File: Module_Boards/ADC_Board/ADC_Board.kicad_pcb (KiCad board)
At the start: 6 copper layers, 13 x 17.7 mm, 46 parts, among them J1 212134-0003, J2 212134-0003, J3 212134-0003, J4 212134-0003, U1 LTC1864LIMS8#PBF, U2 TXB0104RUTR, U3 TPS22916CYFPR, U4 TPS7A9401DSCR, U5 TMUX1104DQAR

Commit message: Big push. Fixed the issues that were pending. See github
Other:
- board text added: "CS"
- board text added: "MI"
- board text added: "SCK"
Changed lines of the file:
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@@
+	)
+	(gr_line
+		(start 130.2 86.5456)
+		(end 129.946 86.5456)
+		(stroke
+			(width 0.1)
+			(type default)
+		)
+		(layer "F.SilkS")
+	)
+	(gr_line
+		(start 140.990235 86.668504)
+		(end 141.334606 87.407011)
+		(stroke
+			(width 0.1)
+			(type default)
+		)
+		(layer "F.SilkS")
+	)
+	(gr_rect
+		(start 129.7 86.0356)
+		(end 129.9 87.0556)
+		(stroke
+			(width 0.1)
+			(type solid)
+		)
+		(fill solid)
+		(layer "F.SilkS")
+	)
+	(gr_line
+		(start 141.184137 87.038926)
+		(end 141.434869 86.788195)
+		(stroke
+			(width 0.1)
+			(type default)
+		)
+		(layer "F.SilkS")
+	)
+	(gr_line
+		(start 140.780535 86.809306)
+		(end 141.124907 87.547813)
+		(stroke
+			(width 0.1)
+			(type default)
+		)
+		(layer "F.SilkS")
+	)
+	(gr_poly
+		(pts
+			(xy 141.60188 89.015667) (xy 141.036196 89.128804) (xy 141.149333 88.56312)
+		)
+		(stroke
+			(width 0.1)
+			(type solid)
+		)
+		(fill solid)
+		(layer "F.SilkS")
+	)
+	(gr_line
+		(start 130.2 87.0536)
+		(end 130.2 86.0376)
+		(stroke
+			(width 0.1)
+			(type default)
+		)
+		(layer "F.SilkS")
+	)
+	(gr_line
+		(start 141.319039 88.845961)
+		(end 141.658449 88.506551)
+		(stroke
+			(width 0.2)
+			(type default)
+		)
+		(layer "F.SilkS")
+	)
+	(gr_line
+		(start 130.454 86.9266)
+		(end 130.454 86.1646)
+		(stroke
+			(width 0.1)
+			(type default)
+		)
+		(layer "F.SilkS")
+	)
+	(gr_line
+		(start 130.708 86.6726)
+		(end 130.708 86.4186)
+		(stroke
+			(width 0.1)
+			(type default)
+		)
+		(layer "F.SilkS")
+	)
+	(gr_rect
+		(start 141.1 84.7656)
+		(end 141.3 85.7856)
+		(stroke
+			(width 0.1)
+			(type solid)
+		)
+		(fill solid)
+		(layer "F.SilkS")
 	)
 	(gr_line
@@
 		)
 		(layer "Edge.Cuts")
+	)
+	(gr_text "CS"
+		(at 130.325269 85.863695 90)
+		(layer "F.SilkS")
+		(effects
+			(font
+				(size 0.5 0.5)
+				(thickness 0.1)
+				(bold yes)
+			)
+			(justify left bottom)
+		)
+	)
+	(gr_text "MI"
+		(at 130.325269 84.510362 90)
+		(layer "F.SilkS")
+		(effects
+			(font
+				(size 0.5 0.5)
+				(thickness 0.1)
+				(bold yes)
+			)
+			(justify left bottom)
+		)
+	)
+	(gr_text "SCK"
+		(at 130.325269 83.573695 90)
+		(layer "F.SilkS")
+		(effects
+			(font
+				(size 0.5 0.5)
+				(thickness 0.1)
+				(bold yes)
+			)
+			(justify left bottom)
+		)
 	)
 	(segment
@@
 		)
 	)
+	(group ""
+		(members "25f6bcfe-40dd-4638-9ee8-8388c1f33a2e" "b8615d0e-870a-46f8-8a8a-49a5995449ec"
+			"c08f6b8e-181b-46dc-a771-4c8004ccd757" "c74e4047-e888-4410-b1a2-d58da0c20ed8"
+		)
+	)

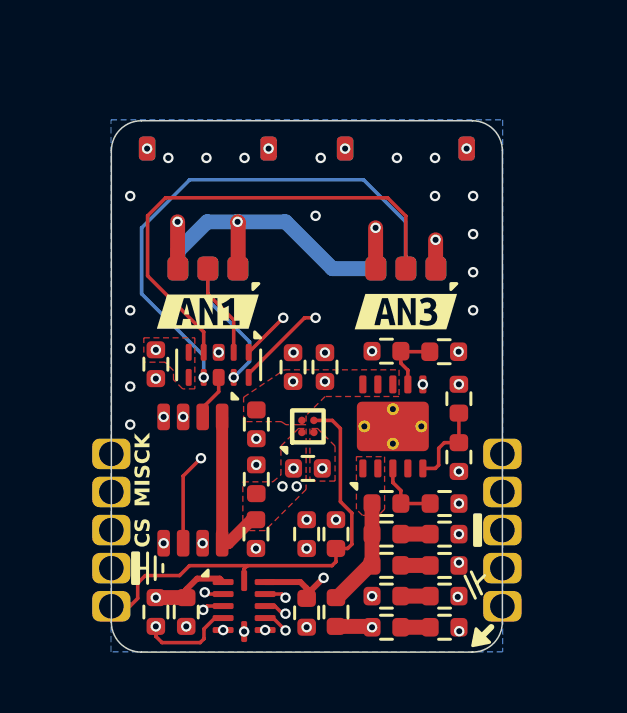
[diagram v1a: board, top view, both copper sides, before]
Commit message: Fixed bugs. Added comments. Push before changing the ADC
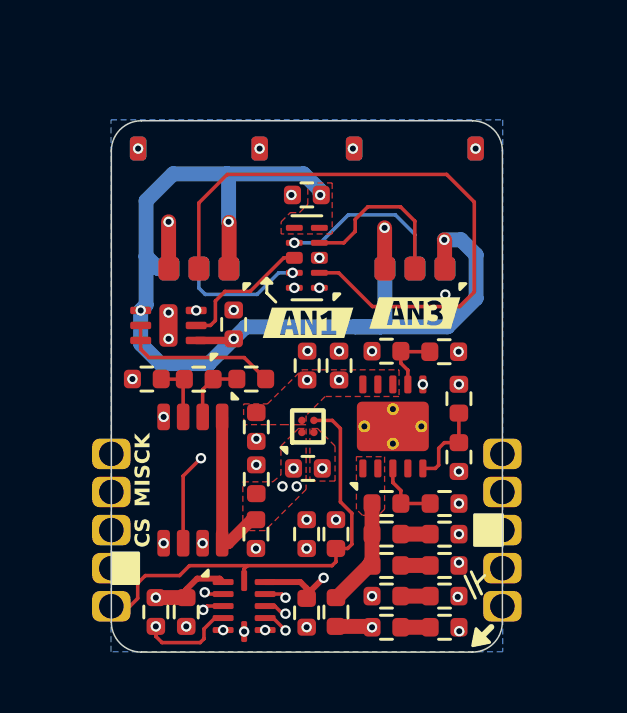
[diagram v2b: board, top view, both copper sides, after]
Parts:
- removed kibuzzard-67164525: G***, kibuzzard-67164525
- removed kibuzzard-6716453A: G***, kibuzzard-6716453A
- added C14: 2n20 25V, X-MODs_PcbLib:C0402, F.Cu at (131.9, 80.2)
- added C15: 100n 10V, X-MODs_PcbLib:C0402, F.Cu at (133.1, 78.4)
- added R1: 39R0, X-MODs_PcbLib:R0402, F.Cu at (130.2, 80.2)
- added R3: 39R0, X-MODs_PcbLib:R0402, F.Cu at (133.7, 80.2)
- added U6: LTC6255CS6#TRMPBF, X-MODs_PcbLib:DFN-6, F.Cu at (130.9, 78.5)
- added kibuzzard-674D683C: G***, kibuzzard-674D683C, F.Cu at (135.5, 78.4)
- added kibuzzard-674D6840: G***, kibuzzard-674D6840, F.Cu at (139.1, 78.0)
- C1: value 10u0 16V -> 2u20 16V
- C10, C6, C8: value 10u0 16V -> 22u0 6V3
- C7, C9: value 10u0 16V -> 10n0 16V
- FB1: value FerriteBead -> 300R
- R10, R12: value TBD -> 1R00
- R11, R9: value TBD -> 0R30
- R13, R15: value TBD -> 100K
- R7: value TBD -> 169K
- R8: value TBD -> 1M33
- moved C12 7.56 mm to (135.5, 74.1), turned to 180 degrees
- moved U5 4.62 mm to (135.5, 76.2), turned to 180 degrees
- moved C10 0.47 mm to (136.6, 79.8)
- moved C4 0.47 mm to (135.5, 79.8)
- moved J1 0.30 mm to (131.9, 76.6)
- moved J2 0.30 mm to (131.9, 76.6)
- moved J3 0.30 mm to (139.1, 76.6)
- moved J4 0.30 mm to (139.1, 76.6)
- moved kibuzzard-67164A85 0.30 mm to (139.1, 78.0)
- moved kibuzzard-67164A89 0.30 mm to (131.9, 78.0)
- moved R6 0.09 mm to (133.8, 81.8)
- turned FB1 to 90 degrees
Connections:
- FB1 pad 1: /[1] Power Regulation & Level Shifting/+3V3_FILT -> +3V3
- FB1 pad 2: +3V3 -> /[1] Power Regulation & Level Shifting/+3V3_FILT
- J5 pad 10: MUX_A1 -> MUX_A0
- J5 pad 9: MUX_A0 -> MUX_A1
- U1 pad 3: GND -> Net-(U1-IN-)
- U5 pad 8: /[2] ADC & Multiplexer/ADC_IN -> /[2] ADC & Multiplexer/BUFFER_IN
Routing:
- net /[2] ADC & Multiplexer/AN_1: track 3.15 -> 21.0 mm
- net +3VA_ADC: track 39.4 -> 54.3 mm, vias 6 -> 8
- net /[2] ADC & Multiplexer/AN_4: track 17.5 -> 5.81 mm
- net /[2] ADC & Multiplexer/AN_3: track 16.2 -> 5.75 mm
- net /[2] ADC & Multiplexer/CHARGE_BUCKET_IN: track 0.00 -> 5.37 mm
- net /[2] ADC & Multiplexer/BUFFER_IN: track 0.00 -> 4.59 mm
- net MUX_A0: track 13.6 -> 9.67 mm
- net Net-(U1-IN-): track 0.00 -> 2.05 mm
- net MUX_A1: track 13.8 -> 12.5 mm
- net /[2] ADC & Multiplexer/ADC_IN: track 1.54 -> 2.19 mm
- net GND: track 2.91 -> 2.90 mm, vias 47 -> 35

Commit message: Added new version of the ADC Board. Better ADC, precision reference. Similar power consumption
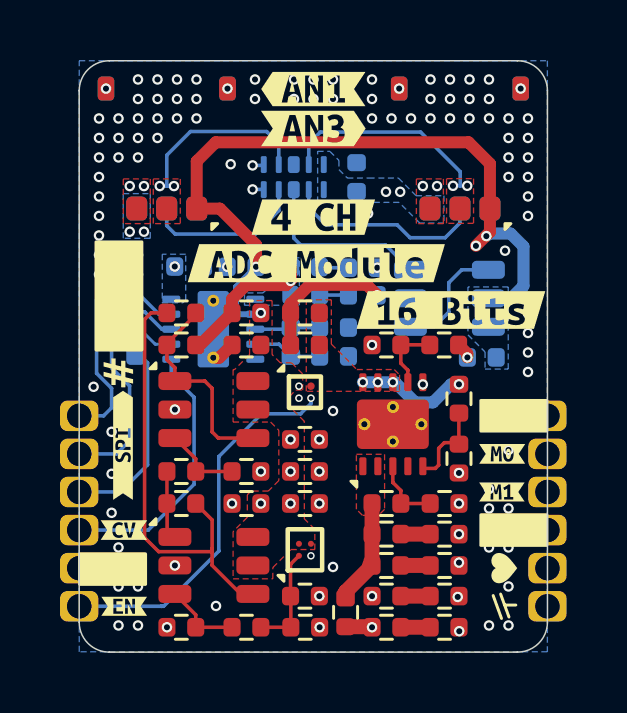
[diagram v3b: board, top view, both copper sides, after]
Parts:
- removed C2: 100n 10V, X-MODs_PcbLib:C0402
- removed kibuzzard-671559FE: G***, kibuzzard-671559FE
- removed kibuzzard-67164A85: G***, kibuzzard-67164A85
- removed kibuzzard-67164A89: G***, kibuzzard-67164A89
- removed kibuzzard-674D683C: G***, kibuzzard-674D683C
- removed kibuzzard-674D6840: G***, kibuzzard-674D6840
- added C16: 1u00 10V, X-MODs_PcbLib:C0402, F.Cu at (131.3, 88.5)
- added C17: 1u00 10V, X-MODs_PcbLib:C0402, F.Cu at (131.3, 84.4)
- added C18: 1u00 10V, X-MODs_PcbLib:C0402, F.Cu at (135.4, 83.3)
- added C20: 100n 10V, X-MODs_PcbLib:C0402, F.Cu at (135.4, 84.4)
- added C21: 10u0 4V, X-MODs_PcbLib:C0402, F.Cu at (135.4, 87.5)
- added C22: 22u0 6V3, X-MODs_PcbLib:C0402, B.Cu at (137.4, 76.5)
- added C23: 100n 10V, X-MODs_PcbLib:C0402, B.Cu at (137.4, 77.5)
- added C24: 100n 10V, X-MODs_PcbLib:C0402, F.Cu at (133.5, 84.4)
- added C25: 100n 10V, X-MODs_PcbLib:C0402, F.Cu at (133.5, 79.1)
- added C26: 100n 10V, X-MODs_PcbLib:C0402, F.Cu at (135.5, 88.5)
- added G***: LOGO, LOGO, F.Cu at (141.0, 86.8)
- added R16: 0R15, X-MODs_PcbLib:R0402, B.Cu at (135.5, 76.5)
- added R17: 0R15, X-MODs_PcbLib:R0402, B.Cu at (135.5, 77.4)
- added R18: 0R00, X-MODs_PcbLib:R0402, F.Cu at (131.3, 79.1)
- added R19: 0R00, X-MODs_PcbLib:R0402, F.Cu at (133.5, 78.0)
- added U7: OPA310SIDBVR, X-MODs_PcbLib:SOT_23_5_SHDN, F.Cu at (132.4, 81.3)
- added U8: OPA333AIDBVR, X-MODs_PcbLib:SOT_23_5_SHDN, F.Cu at (132.4, 86.5)
- added kibuzzard-6751DE44: G***, kibuzzard-6751DE44, F.Cu at (129.4, 85.3)
- added kibuzzard-6751DE4C: G***, kibuzzard-6751DE4C, F.Cu at (129.4, 82.5)
- added kibuzzard-6751DFCA: G***, kibuzzard-6751DFCA, F.Cu at (142.0, 82.7)
- added kibuzzard-6751DFD0: G***, kibuzzard-6751DFD0, F.Cu at (142.0, 84.0)
- added kibuzzard-6751E059: G***, kibuzzard-6751E059, F.Cu at (129.4, 87.8)
- added kibuzzard-6751E0AA: G***, kibuzzard-6751E0AA, B.Cu at (135.7, 70.6)
- added kibuzzard-6751E0C1: G***, kibuzzard-6751E0C1, B.Cu at (135.7, 71.9)
- added kibuzzard-6751E0F0: G***, kibuzzard-6751E0F0, F.Cu at (135.7, 70.6)
- added kibuzzard-6751E0F4: G***, kibuzzard-6751E0F4, F.Cu at (135.7, 71.9)
- added kibuzzard-6751E246: G***, kibuzzard-6751E246, F.Cu at (135.7, 74.8)
- added kibuzzard-6751E260: G***, kibuzzard-6751E260, F.Cu at (140.3, 77.9)
- added kibuzzard-6751F13D: G***, kibuzzard-6751F13D, F.Cu at (135.8, 76.4)
- C1, C12, C15, R1, R2, R3, U5: moved to B.Cu
- C14: value 2n20 25V -> 680p 50V; moved to B.Cu
- C3: value 100n 10V -> 2u20 16V; moved to B.Cu
- C5: value 100n 10V -> 1u00 10V
- R4: value 1M00 -> 1K00
- R5: value 56K0 -> 1K00
- R6: value 56K0 -> 20K0
- U1: value LTC1864LIMS8#PBF -> ADS8860IDRCT; footprint X-MODs_PcbLib:MSOP-8 -> X-MODs_PcbLib:VSON-10_3x3mm_P0.5; moved to B.Cu
- U2: value TXB0104RUTR -> REF35250YBHR; footprint X-MODs_PcbLib:UQFN-12_1.7x2mm -> X-MODs_PcbLib:DSBGA-4_1.085x0.870mm
- U6: value LTC6255CS6#TRMPBF -> LTC6255IDC#TRMPBF; footprint X-MODs_PcbLib:DFN-6 -> X-MODs_PcbLib:SOT_23_6; moved to B.Cu
- moved C3 11.5 mm to (131.6, 76.5), turned to 0 degrees
- moved U6 9.41 mm to (140.3, 77.5), turned to 0 degrees
- moved R2 8.57 mm to (129.8, 79.0), turned to -90 degrees
- moved C15 8.34 mm to (141.3, 79.5), turned to 180 degrees
- moved C1 7.10 mm to (133.3, 76.5), turned to 180 degrees
- moved R1 6.29 mm to (136.4, 79.5), turned to 180 degrees
- moved R4 5.56 mm to (131.3, 83.3), turned to 0 degrees
- moved C5 5.12 mm to (133.5, 83.3), turned to 0 degrees
- moved U1 5.07 mm to (132.4, 78.6), turned to 180 degrees
- moved R6 4.55 mm to (131.3, 78.0), turned to 0 degrees
- moved C14 3.31 mm to (135.0, 79.0), turned to -90 degrees
- moved R3 3.25 mm to (136.4, 78.5)
- moved R5 3.06 mm to (133.5, 88.5), turned to 180 degrees
- moved U2 2.76 mm to (135.4, 85.9), turned to 90 degrees
- moved U5 2.73 mm to (135.1, 73.5), turned to -90 degrees
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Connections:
- C14 pad 1: /[2] ADC & Multiplexer/ADC_IN -> /[2] ADC & Multiplexer/ADC_IN_P
- C14 pad 2: Net-(U1-IN-) -> /[2] ADC & Multiplexer/ADC_IN_N
- C5 pad 1: +3VA -> Net-(U7-+)
- J5 pad 1: SPI_SCK_1V8 -> ~{ADC_CS}
- J5 pad 10: MUX_A0 -> MUX_A1
- J5 pad 2: SPI_MISO_1V8 -> ADC_SCK
- J5 pad 3: SPI_CS_1V8 -> ADC_MISO
- J5 pad 4: GND -> ADC_CONV
- J5 pad 5: ADC_EN -> GND
- J5 pad 6: +3V3 -> ADC_EN
- J5 pad 7: +1V8 -> +3V3
- J5 pad 8: GND -> +1V8
- J5 pad 9: MUX_A1 -> GND
- R1 pad 2: Net-(U1-IN-) -> /[2] ADC & Multiplexer/ADC_IN_N
- R2 pad 1: Net-(U1-SDO) -> Net-(U1-DOUT)
- R2 pad 2: SPI_MISO_3V -> ADC_MISO
- R3 pad 2: /[2] ADC & Multiplexer/ADC_IN -> /[2] ADC & Multiplexer/ADC_IN_P
- R4 pad 1: GND -> Net-(U8-VOUT)
- R4 pad 2: ADC_EN -> Net-(U7-+)
- R5 pad 1: +1V8 -> /[2] ADC & Multiplexer/REF_OUT
- R5 pad 2: SPI_CS_1V8 -> Net-(U8-+)
- R6 pad 1: +3VA -> Net-(U8--)
- R6 pad 2: SPI_CS_3V -> Net-(U7--)
- U1 pad 1: +3VA_ADC -> +VREF
- U1 pad 2: /[2] ADC & Multiplexer/ADC_IN -> +3VA_ADC
- U1 pad 3: Net-(U1-IN-) -> /[2] ADC & Multiplexer/ADC_IN_P
- U1 pad 4: GND -> /[2] ADC & Multiplexer/ADC_IN_N
- U1 pad 5: SPI_CS_3V -> GND
- U1 pad 6: Net-(U1-SDO) -> ADC_CONV
- U1 pad 7: SPI_SCK_3V -> Net-(U1-DOUT)
- U1 pad 8: +3VA_ADC -> ADC_SCK
- U6 pad 1: +3VA_ADC -> /[2] ADC & Multiplexer/CHARGE_BUCKET_IN
- U6 pad 2: /[2] ADC & Multiplexer/BUFFER_IN -> GND
- U6 pad 3: GND -> /[2] ADC & Multiplexer/BUFFER_IN
- U6 pad 4: +3VA_ADC -> /[2] ADC & Multiplexer/CHARGE_BUCKET_IN
- U6 pad 5: /[2] ADC & Multiplexer/CHARGE_BUCKET_IN -> +3VA_ADC
- U6 pad 6: /[2] ADC & Multiplexer/CHARGE_BUCKET_IN -> +3VA_ADC
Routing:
- net SPI_CS_3V: track 19.4 -> 0.00 mm, vias 3 -> 0
- net Net-(U8--): track 0.00 -> 14.7 mm
- net /[2] ADC & Multiplexer/AN_1: track 21.0 -> 6.43 mm, vias 0 -> 2
- net +3VA: track 16.0 -> 3.73 mm
- net ADC_CONV: track 0.00 -> 8.95 mm
- net ADC_SCK: track 0.00 -> 8.43 mm
- net Net-(U1-SDO): track 8.06 -> 0.00 mm, vias 2 -> 0
- net ~{ADC_CS}: track 0.00 -> 8.02 mm
- net SPI_SCK_1V8: track 7.61 -> 0.00 mm, vias 1 -> 0
- net SPI_CS_1V8: track 7.51 -> 0.00 mm, vias 1 -> 0
- net Net-(U7--): track 0.00 -> 7.01 mm
- net ADC_MISO: track 0.00 -> 6.74 mm
- net SPI_MISO_1V8: track 6.64 -> 0.00 mm, vias 1 -> 0
- net SPI_MISO_3V: track 6.26 -> 0.00 mm, vias 2 -> 0
- net +1V8: track 15.4 -> 21.6 mm
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- added copper zone on B.Cu, net +1V8
- added copper zone on B.Cu, net +3VA_ADC
- added copper zone on B.Cu, net +VREF
- added copper zone on F.Cu, net /[2] ADC & Multiplexer/AN_1
- added copper zone on F.Cu, net /[2] ADC & Multiplexer/AN_3
- added copper zone on In4.Cu, net GND
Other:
- board size 13 x 17.7 mm -> 15.6 x 19.7 mm
- board text added: "#"
- board text removed: "CS"
- board text removed: "MI"
- board text removed: "SCK"

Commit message: Final revision and production files
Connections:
- net /[1] Power Regulation & Level Shifting/+3V3_FILT renamed /[1] Power Regulation & Connectors/+3V3_FILT
- net /[1] Power Regulation & Level Shifting/EN_UV renamed /[1] Power Regulation & Connectors/EN_UV
- net /[1] Power Regulation & Level Shifting/FB_PG renamed /[1] Power Regulation & Connectors/FB_PG
- net /[1] Power Regulation & Level Shifting/NR/SS renamed /[1] Power Regulation & Connectors/NR/SS
- net /[2] ADC & Multiplexer/ADC_IN_N renamed /[2] ADC, Multiplexer & Reference/ADC_IN_N
- net /[2] ADC & Multiplexer/ADC_IN_P renamed /[2] ADC, Multiplexer & Reference/ADC_IN_P
- net /[2] ADC & Multiplexer/AN_1 renamed /[2] ADC, Multiplexer & Reference/AN_1
- net /[2] ADC & Multiplexer/AN_2 renamed /[2] ADC, Multiplexer & Reference/AN_2
- net /[2] ADC & Multiplexer/AN_3 renamed /[2] ADC, Multiplexer & Reference/AN_3
- net /[2] ADC & Multiplexer/AN_4 renamed /[2] ADC, Multiplexer & Reference/AN_4
- net /[2] ADC & Multiplexer/BUFFER_IN renamed /[2] ADC, Multiplexer & Reference/BUFFER_IN
- net /[2] ADC & Multiplexer/CHARGE_BUCKET_IN renamed /[2] ADC, Multiplexer & Reference/CHARGE_BUCKET_IN
- net /[2] ADC & Multiplexer/REF_OUT renamed /[2] ADC, Multiplexer & Reference/REF_OUT
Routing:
- net Net-(U8--): track 14.7 -> 12.1 mm
- net GND: vias 137 -> 136
